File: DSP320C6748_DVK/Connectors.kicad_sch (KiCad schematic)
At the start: 12 parts, among them J14 Conn_02x25_Odd_Even, J15 Conn_02x10_Odd_Even, J16 Conn_02x10_Odd_Even, J17 Conn_02x25_Odd_Even, J18 525593652, J19 Conn_01x02_Pin, J20 Conn_01x02_Pin, J21 Conn_01x02_Pin, J22 UART_{1}, J23 UART_{2}

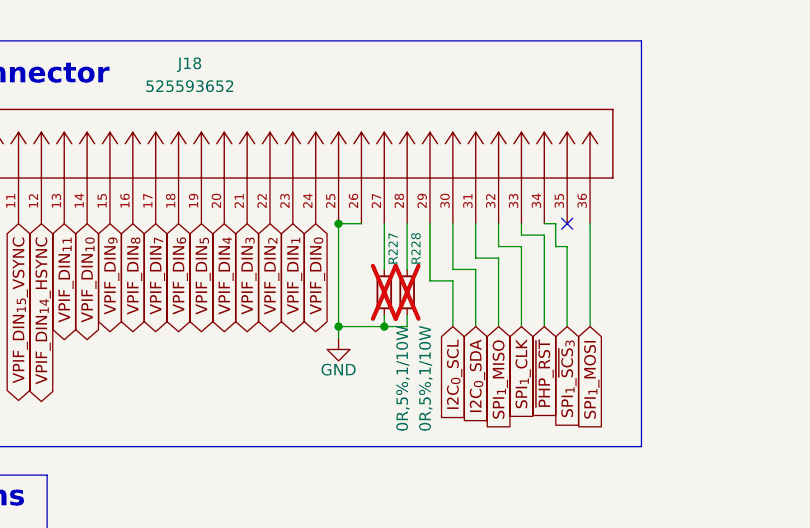
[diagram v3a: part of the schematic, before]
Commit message: Scheamtic Re-annotation done, Some footprints assigned
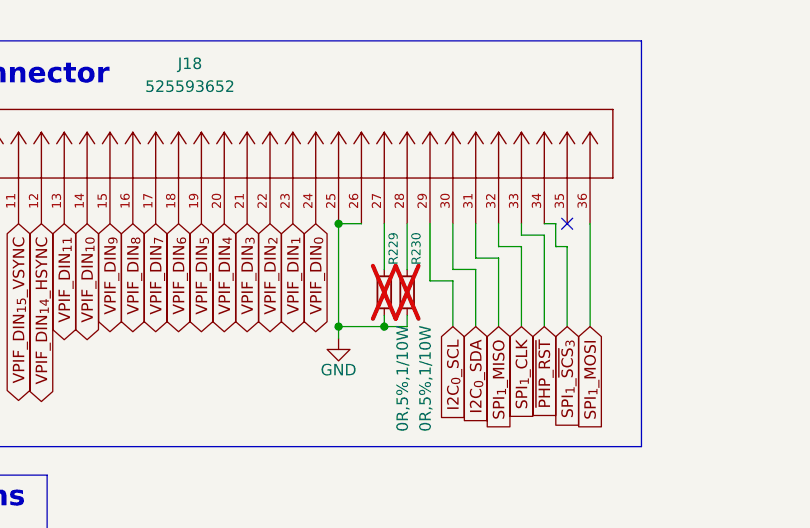
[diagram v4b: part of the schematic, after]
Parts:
- R229: renamed from R227; footprint (none) -> Resistor_SMD:R_0603_1608Metric_Pad0.98x0.95mm_HandSolder
- R230: renamed from R228; footprint (none) -> Resistor_SMD:R_0603_1608Metric_Pad0.98x0.95mm_HandSolder
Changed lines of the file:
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@@
 		(in_pos_files yes)
 		(dnp no)
-		(property "Reference" "#PWR0365"
+		(property "Reference" "#PWR0369"
 			(at 102.87 83.82 0)
 			(hide yes)
@@
 			(project "DSP320C6748_DVK"
 				(path "/3a70ffc0-9fe7-4a5b-b3c2-23140355df82/5c92834a-e218-4842-9f37-78ba42443e32"
-					(reference "#PWR0365")
+					(reference "#PWR0369")
 					(unit 1)
 				)
@@
 		(in_pos_files yes)
 		(dnp no)
-		(property "Reference" "#PWR0359"
+		(property "Reference" "#PWR0363"
 			(at 39.37 101.6 0)
 			(hide yes)
@@
 			(project "DSP320C6748_DVK"
 				(path "/3a70ffc0-9fe7-4a5b-b3c2-23140355df82/5c92834a-e218-4842-9f37-78ba42443e32"
-					(reference "#PWR0359")
+					(reference "#PWR0363")
 					(unit 1)
 				)
@@
 		(in_pos_files yes)
 		(dnp no)
-		(property "Reference" "#PWR0364"
+		(property "Reference" "#PWR0368"
 			(at 100.33 129.54 0)
 			(hide yes)
@@
 			(project "DSP320C6748_DVK"
 				(path "/3a70ffc0-9fe7-4a5b-b3c2-23140355df82/5c92834a-e218-4842-9f37-78ba42443e32"
-					(reference "#PWR0364")
+					(reference "#PWR0368")
 					(unit 1)
 				)
@@
 		(in_pos_files yes)
 		(dnp no)
-		(property "Reference" "#PWR0358"
+		(property "Reference" "#PWR0362"
 			(at 26.67 64.77 0)
 			(hide yes)
@@
 			(project "DSP320C6748_DVK"
 				(path "/3a70ffc0-9fe7-4a5b-b3c2-23140355df82/5c92834a-e218-4842-9f37-78ba42443e32"
-					(reference "#PWR0358")
+					(reference "#PWR0362")
 					(unit 1)
 				)
@@
 		(in_pos_files yes)
 		(dnp no)
-		(property "Reference" "#PWR0366"
+		(property "Reference" "#PWR0370"
 			(at 109.22 30.48 0)
 			(hide yes)
@@
 			(project "DSP320C6748_DVK"
 				(path "/3a70ffc0-9fe7-4a5b-b3c2-23140355df82/5c92834a-e218-4842-9f37-78ba42443e32"
-					(reference "#PWR0366")
+					(reference "#PWR0370")
 					(unit 1)
 				)
@@
 		(in_pos_files yes)
 		(dnp no)
-		(property "Reference" "#PWR0360"
+		(property "Reference" "#PWR0364"
 			(at 54.61 165.1 0)
 			(hide yes)
@@
 			(project "DSP320C6748_DVK"
 				(path "/3a70ffc0-9fe7-4a5b-b3c2-23140355df82/5c92834a-e218-4842-9f37-78ba42443e32"
-					(reference "#PWR0360")
+					(reference "#PWR0364")
 					(unit 1)
 				)
@@
 		(in_pos_files yes)
 		(dnp no)
-		(property "Reference" "#PWR0393"
+		(property "Reference" "#PWR0381"
 			(at 241.3 110.49 0)
 			(hide yes)
@@
 			(project "DSP320C6748_DVK"
 				(path "/3a70ffc0-9fe7-4a5b-b3c2-23140355df82/5c92834a-e218-4842-9f37-78ba42443e32"
-					(reference "#PWR0393")
+					(reference "#PWR0381")
 					(unit 1)
 				)
@@
 		(in_pos_files yes)
 		(dnp yes)
-		(property "Reference" "R227"
+		(property "Reference" "R229"
 			(at 238.506 43.942 90)
 			(show_name no)
@@
 			)
 		)
-		(property "Footprint" ""
+		(property "Footprint" "Resistor_SMD:R_0603_1608Metric_Pad0.98x0.95mm_HandSolder"
 			(at 237.49 46.99 0)
 			(hide yes)
@@
 			(project "DSP320C6748_DVK"
 				(path "/3a70ffc0-9fe7-4a5b-b3c2-23140355df82/5c92834a-e218-4842-9f37-78ba42443e32"
-					(reference "R227")
+					(reference "R229")
 					(unit 1)
 				)
@@
 		(in_pos_files yes)
 		(dnp no)
-		(property "Reference" "#PWR0371"
+		(property "Reference" "#PWR0375"
 			(at 135.89 29.21 0)
 			(hide yes)
@@
 			(project "DSP320C6748_DVK"
 				(path "/3a70ffc0-9fe7-4a5b-b3c2-23140355df82/5c92834a-e218-4842-9f37-78ba42443e32"
-					(reference "#PWR0371")
+					(reference "#PWR0375")
 					(unit 1)
 				)
@@
 		(in_pos_files yes)
 		(dnp yes)
-		(property "Reference" "R228"
+		(property "Reference" "R230"
 			(at 241.046 43.942 90)
 			(show_name no)
@@
 			)
 		)
-		(property "Footprint" ""
+		(property "Footprint" "Resistor_SMD:R_0603_1608Metric_Pad0.98x0.95mm_HandSolder"
 			(at 240.03 46.99 0)
 			(hide yes)
@@
 			(project "DSP320C6748_DVK"
 				(path "/3a70ffc0-9fe7-4a5b-b3c2-23140355df82/5c92834a-e218-4842-9f37-78ba42443e32"
-					(reference "R228")
+					(reference "R230")
 					(unit 1)
 				)
@@
 		(in_pos_files yes)
 		(dnp no)
-		(property "Reference" "#PWR0363"
+		(property "Reference" "#PWR0367"
 			(at 77.47 88.9 0)
 			(hide yes)
@@
 			(project "DSP320C6748_DVK"
 				(path "/3a70ffc0-9fe7-4a5b-b3c2-23140355df82/5c92834a-e218-4842-9f37-78ba42443e32"
-					(reference "#PWR0363")
+					(reference "#PWR0367")
 					(unit 1)
 				)
@@
 		(in_pos_files yes)
 		(dnp no)
-		(property "Reference" "#PWR0362"
+		(property "Reference" "#PWR0366"
 			(at 69.85 64.77 0)
 			(hide yes)
@@
 			(project "DSP320C6748_DVK"
 				(path "/3a70ffc0-9fe7-4a5b-b3c2-23140355df82/5c92834a-e218-4842-9f37-78ba42443e32"
-					(reference "#PWR0362")
+					(reference "#PWR0366")
 					(unit 1)
 				)
@@
 		(in_pos_files yes)
 		(dnp no)
-		(property "Reference" "#PWR0373"
+		(property "Reference" "#PWR0377"
 			(at 171.45 40.64 0)
 			(hide yes)
@@
 			(project "DSP320C6748_DVK"
 				(path "/3a70ffc0-9fe7-4a5b-b3c2-23140355df82/5c92834a-e218-4842-9f37-78ba42443e32"
-					(reference "#PWR0373")
+					(reference "#PWR0377")
 					(unit 1)
 				)
@@
 		(in_pos_files yes)
 		(dnp no)
-		(property "Reference" "#PWR0375"
+		(property "Reference" "#PWR0379"
 			(at 232.41 58.42 0)
 			(hide yes)
@@
 			(project "DSP320C6748_DVK"
 				(path "/3a70ffc0-9fe7-4a5b-b3c2-23140355df82/5c92834a-e218-4842-9f37-78ba42443e32"
-					(reference "#PWR0375")
+					(reference "#PWR0379")
 					(unit 1)
 				)
@@
 		(in_pos_files yes)
 		(dnp no)
-		(property "Reference" "#PWR0372"
+		(property "Reference" "#PWR0376"
 			(at 156.21 60.96 0)
 			(hide yes)
@@
 			(project "DSP320C6748_DVK"
 				(path "/3a70ffc0-9fe7-4a5b-b3c2-23140355df82/5c92834a-e218-4842-9f37-78ba42443e32"
-					(reference "#PWR0372")
+					(reference "#PWR0376")
 					(unit 1)
 				)
@@
 		(in_pos_files yes)
 		(dnp no)
-		(property "Reference" "#PWR0357"
+		(property "Reference" "#PWR0361"
 			(at 25.4 88.9 0)
 			(hide yes)
@@
 			(project "DSP320C6748_DVK"
 				(path "/3a70ffc0-9fe7-4a5b-b3c2-23140355df82/5c92834a-e218-4842-9f37-78ba42443e32"
-					(reference "#PWR0357")
+					(reference "#PWR0361")
 					(unit 1)
 				)
@@
 		(in_pos_files yes)
 		(dnp no)
-		(property "Reference" "#PWR0370"
+		(property "Reference" "#PWR0374"
 			(at 129.54 90.17 0)
 			(hide yes)
@@
 			(project "DSP320C6748_DVK"
 				(path "/3a70ffc0-9fe7-4a5b-b3c2-23140355df82/5c92834a-e218-4842-9f37-78ba42443e32"
-					(reference "#PWR0370")
+					(reference "#PWR0374")
 					(unit 1)
 				)
@@
 		(in_pos_files yes)
 		(dnp no)
-		(property "Reference" "#PWR0368"
+		(property "Reference" "#PWR0372"
 			(at 113.03 163.83 0)
 			(hide yes)
@@
 			(project "DSP320C6748_DVK"
 				(path "/3a70ffc0-9fe7-4a5b-b3c2-23140355df82/5c92834a-e218-4842-9f37-78ba42443e32"
-					(reference "#PWR0368")
+					(reference "#PWR0372")
 					(unit 1)
 				)
@@
 		(in_pos_files yes)
 		(dnp no)
-		(property "Reference" "#PWR0374"
+		(property "Reference" "#PWR0378"
 			(at 182.88 48.26 0)
 			(hide yes)
@@
 			(project "DSP320C6748_DVK"
 				(path "/3a70ffc0-9fe7-4a5b-b3c2-23140355df82/5c92834a-e218-4842-9f37-78ba42443e32"
-					(reference "#PWR0374")
+					(reference "#PWR0378")
 					(unit 1)
 				)
@@
 		(in_pos_files yes)
 		(dnp no)
-		(property "Reference" "#PWR0361"
+		(property "Reference" "#PWR0365"
 			(at 57.15 101.6 0)
 			(hide yes)
@@
 			(project "DSP320C6748_DVK"
 				(path "/3a70ffc0-9fe7-4a5b-b3c2-23140355df82/5c92834a-e218-4842-9f37-78ba42443e32"
-					(reference "#PWR0361")
+					(reference "#PWR0365")
 					(unit 1)
 				)
@@
 		(in_pos_files yes)
 		(dnp no)
-		(property "Reference" "#PWR0392"
+		(property "Reference" "#PWR0380"
 			(at 241.3 93.98 0)
 			(hide yes)
@@
 			(project "DSP320C6748_DVK"
 				(path "/3a70ffc0-9fe7-4a5b-b3c2-23140355df82/5c92834a-e218-4842-9f37-78ba42443e32"
-					(reference "#PWR0392")
+					(reference "#PWR0380")
 					(unit 1)
 				)
@@
 		(in_pos_files yes)
 		(dnp no)
-		(property "Reference" "#PWR0367"
+		(property "Reference" "#PWR0371"
 			(at 109.22 93.98 0)
 			(hide yes)
@@
 			(project "DSP320C6748_DVK"
 				(path "/3a70ffc0-9fe7-4a5b-b3c2-23140355df82/5c92834a-e218-4842-9f37-78ba42443e32"
-					(reference "#PWR0367")
+					(reference "#PWR0371")
 					(unit 1)
 				)
@@
 		(in_pos_files yes)
 		(dnp no)
-		(property "Reference" "#PWR0369"
+		(property "Reference" "#PWR0373"
 			(at 116.84 90.17 0)
 			(hide yes)
@@
 			(project "DSP320C6748_DVK"
 				(path "/3a70ffc0-9fe7-4a5b-b3c2-23140355df82/5c92834a-e218-4842-9f37-78ba42443e32"
-					(reference "#PWR0369")
+					(reference "#PWR0373")
 					(unit 1)
 				)
